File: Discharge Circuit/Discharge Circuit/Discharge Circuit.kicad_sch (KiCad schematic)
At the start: 6 parts, among them J1 MPT-02-01-XX-X-RA-SD, J2 IPBT-102-H1-T-S-RA-K, J3 PET-02-01-T-VT-LC, K2 FTR-E1AA012Y-GR

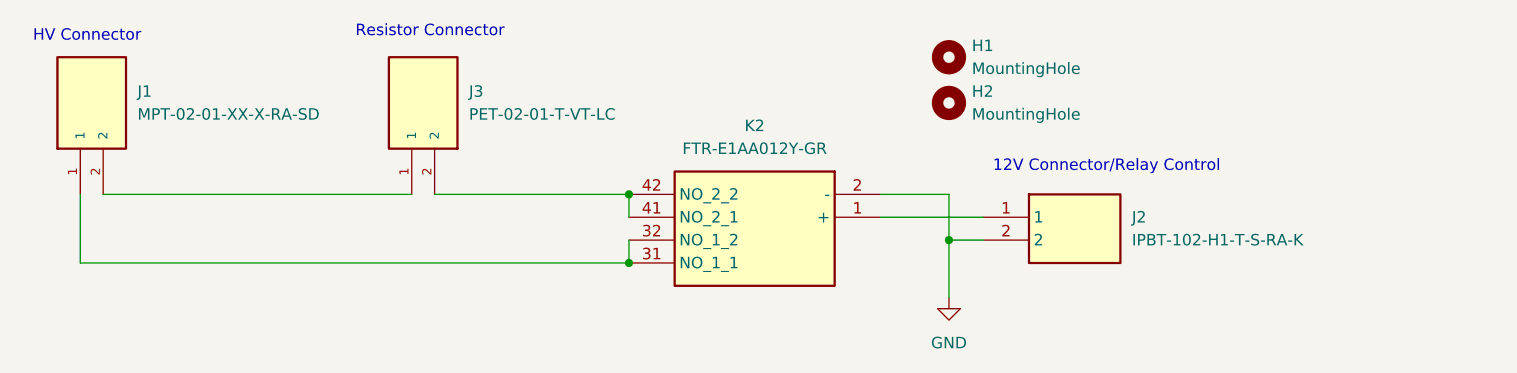
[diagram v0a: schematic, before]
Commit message: Added flyback diode
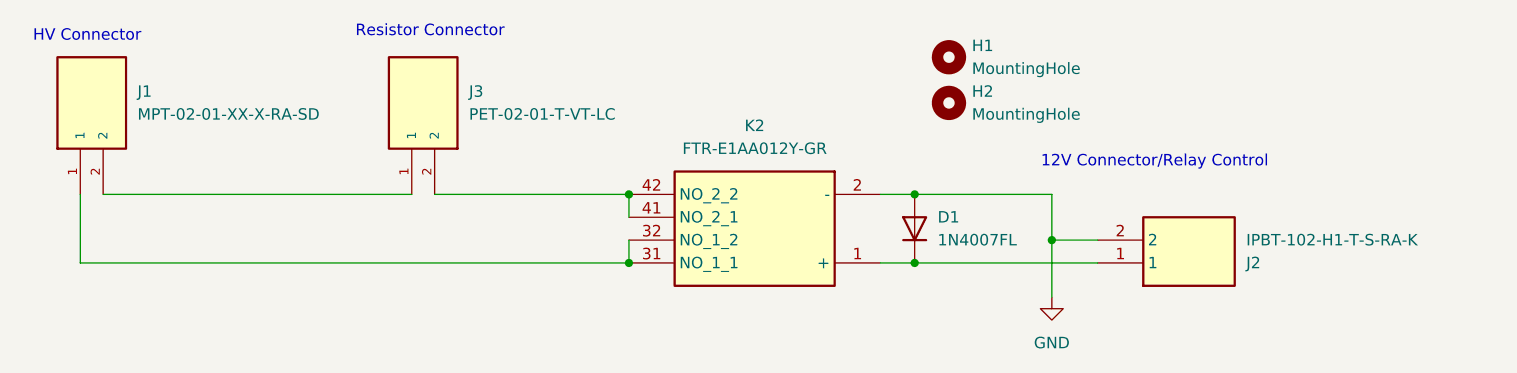
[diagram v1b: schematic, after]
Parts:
- added D1: 1N4007FL, Diode_SMD:D_SOD-123F, symbol Device:D
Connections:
- net GND: now also D1.2 (A)
- net at J2.1, K2.1 (+): now also D1.1 (K)
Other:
- moved on the sheet: J2
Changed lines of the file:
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@@
 	(text "12V Connector/Relay Control\n\n"
 		(exclude_from_sim no)
-		(at 183.896 108.458 0)
+		(at 189.23 107.95 0)
 		(effects
 			(font
@@
 	)
 	(junction
-		(at 166.37 115.57)
+		(at 130.81 118.11)
 		(diameter 0)
 		(color 0 0 0 0)
 	)
 	(junction
-		(at 130.81 118.11)
+		(at 177.8 115.57)
+		(diameter 0)
+		(color 0 0 0 0)
+	)
+	(junction
+		(at 162.56 118.11)
 		(diameter 0)
 		(color 0 0 0 0)
@@
 		(color 0 0 0 0)
 	)
+	(junction
+		(at 162.56 110.49)
+		(diameter 0)
+		(color 0 0 0 0)
+	)
+	(wire
+		(pts
+			(xy 162.56 118.11) (xy 182.88 118.11)
+		)
+		(stroke
+			(width 0)
+			(type default)
+		)
+	)
 	(wire
 		(pts
@@
 	(wire
 		(pts
-			(xy 170.18 115.57) (xy 166.37 115.57)
+			(xy 158.75 118.11) (xy 162.56 118.11)
 		)
 		(stroke
@@
 	(wire
 		(pts
-			(xy 158.75 110.49) (xy 166.37 110.49)
-		)
-		(stroke
-			(width 0)
-			(type default)
-		)
-	)
-	(wire
-		(pts
-			(xy 166.37 115.57) (xy 166.37 121.92)
-		)
-		(stroke
-			(width 0)
-			(type default)
-		)
-	)
-	(wire
-		(pts
-			(xy 158.75 113.03) (xy 170.18 113.03)
+			(xy 177.8 115.57) (xy 177.8 121.92)
+		)
+		(stroke
+			(width 0)
+			(type default)
+		)
+	)
+	(wire
+		(pts
+			(xy 158.75 110.49) (xy 162.56 110.49)
 		)
 		(stroke
@@
 	(wire
 		(pts
-			(xy 166.37 110.49) (xy 166.37 115.57)
+			(xy 162.56 110.49) (xy 177.8 110.49)
+		)
+		(stroke
+			(width 0)
+			(type default)
+		)
+	)
+	(wire
+		(pts
+			(xy 177.8 110.49) (xy 177.8 115.57)
+		)
+		(stroke
+			(width 0)
+			(type default)
+		)
+	)
+	(wire
+		(pts
+			(xy 182.88 115.57) (xy 177.8 115.57)
 		)
 		(stroke
@@
 	(symbol
 		(lib_id "power:GND")
-		(at 166.37 121.92 0)
+		(at 177.8 121.92 0)
 		(unit 1)
 		(exclude_from_sim no)
@@
 		(fields_autoplaced yes)
 		(property "Reference" "#PWR01"
-			(at 166.37 128.27 0)
+			(at 177.8 128.27 0)
 			(effects
 				(font
@@
 		)
 		(property "Value" "GND"
-			(at 166.37 127 0)
+			(at 177.8 127 0)
 			(effects
 				(font
@@
 		)
 		(property "Footprint" ""
-			(at 166.37 121.92 0)
+			(at 177.8 121.92 0)
 			(effects
 				(font
@@
 		)
 		(property "Datasheet" ""
-			(at 166.37 121.92 0)
+			(at 177.8 121.92 0)
 			(effects
 				(font
@@
 		)
 		(property "Description" "Power symbol creates a global label with name \"GND\" , ground"
-			(at 166.37 121.92 0)
+			(at 177.8 121.92 0)
 			(effects
 				(font
@@
 	(symbol
 		(lib_id "IPBT-102-H1-T-S-RA-K:IPBT-102-H1-T-S-RA-K")
-		(at 170.18 113.03 0)
+		(at 182.88 118.11 0)
+		(mirror x)
+		(unit 1)
+		(exclude_from_sim no)
+		(in_bom yes)
+		(on_board yes)
+		(dnp no)
+		(property "Reference" "J2"
+			(at 199.39 118.1101 0)
+			(effects
+				(font
+					(size 1.27 1.27)
+				)
+				(justify left)
+			)
+		)
+		(property "Value" "IPBT-102-H1-T-S-RA-K"
+			(at 199.39 115.5701 0)
+			(effects
+				(font
+					(size 1.27 1.27)
+				)
+				(justify left)
+			)
+		)
+		(property "Footprint" "IPBT:IPBT102H1TSRAK"
+			(at 199.39 23.19 0)
+			(effects
+				(font
+					(size 1.27 1.27)
+				)
+				(justify left top)
+				(hide yes)
+			)
+		)
+		(property "Datasheet" "https://suddendocs.samtec.com/prints/ipbt-1xx-xx-xx-s-xx-mkt.pdf?_gl=1*1nu67sl*_gcl_aw*R0NMLjE3MzY1MTU3OTIuQ2p3S0NBaUFwNE84QmhBa0Vpd0FxdjJVcUhrQ1hwTkVVY2dYbERaeHlmb2JUdHluT3BxNDdWZVFxUVNRZUFOZy1nZnhrUVhoSXppT0lob0NpMXdRQXZEX0J3RQ..*_gcl_au*NTMyOTAxMTM3LjE"
+			(at 199.39 -76.81 0)
+			(effects
+				(font
+					(size 1.27 1.27)
+				)
+				(justify left top)
+				(hide yes)
+			)
+		)
+		(property "Description" "Conn Power Mate Terminal Strip HDR 2 POS 4.19mm Solder RA Thru-Hole 2 Terminal 1 Port Automotive Tube"
+			(at 182.88 118.11 0)
+			(effects
+				(font
+					(size 1.27 1.27)
+				)
+				(hide yes)
+			)
+		)
+		(property "Height" "6.88"
+			(at 199.39 -276.81 0)
+			(effects
+				(font
+					(size 1.27 1.27)
+				)
+				(justify left top)
+				(hide yes)
+			)
+		)
+		(property "Mouser Part Number" "200-IPBT102H1TSRAK"
+			(at 199.39 -376.81 0)
+			(effects
+				(font
+					(size 1.27 1.27)
+				)
+				(justify left top)
+				(hide yes)
+			)
+		)
+		(property "Mouser Price/Stock" "https://www.mouser.co.uk/ProductDetail/Samtec/IPBT-102-H1-T-S-RA-K?qs=PB6%2FjmICvI2Ofyjz6y5btA%3D%3D"
+			(at 199.39 -476.81 0)
+			(effects
+				(font
+					(size 1.27 1.27)
+				)
+				(justify left top)
+				(hide yes)
+			)
+		)
+		(property "Manufacturer_Name" "SAMTEC"
+			(at 199.39 -576.81 0)
+			(effects
+				(font
+					(size 1.27 1.27)
+				)
+				(justify left top)
+				(hide yes)
+			)
+		)
+		(property "Manufacturer_Part_Number" "IPBT-102-H1-T-S-RA-K"
+			(at 199.39 -676.81 0)
+			(effects
+				(font
+					(size 1.27 1.27)
+				)
+				(justify left top)
+				(hide yes)
+			)
+		)
+		(pin "1"
+		)
+		(pin "2"
+		)
+		(instances
+			(project ""
+				(path "/faa29c35-f02e-4949-b6d7-f81fa5cf50a8"
+					(reference "J2")
+					(unit 1)
+				)
+			)
+		)
+	)
+	(symbol
+		(lib_id "Device:D")
+		(at 162.56 114.3 90)
 		(unit 1)
 		(exclude_from_sim no)
@@
 		(dnp no)
 		(fields_autoplaced yes)
-		(property "Reference" "J2"
-			(at 186.69 113.0299 0)
-			(effects
-				(font
-					(size 1.27 1.27)
-				)
-				(justify left)
-			)
-		)
-		(property "Value" "IPBT-102-H1-T-S-RA-K"
-			(at 186.69 115.5699 0)
-			(effects
-				(font
-					(size 1.27 1.27)
-				)
-				(justify left)
-			)
-		)
-		(property "Footprint" "IPBT:IPBT102H1TSRAK"
-			(at 186.69 207.95 0)
-			(effects
-				(font
-					(size 1.27 1.27)
-				)
-				(justify left top)
-				(hide yes)
-			)
-		)
-		(property "Datasheet" "https://suddendocs.samtec.com/prints/ipbt-1xx-xx-xx-s-xx-mkt.pdf?_gl=1*1nu67sl*_gcl_aw*R0NMLjE3MzY1MTU3OTIuQ2p3S0NBaUFwNE84QmhBa0Vpd0FxdjJVcUhrQ1hwTkVVY2dYbERaeHlmb2JUdHluT3BxNDdWZVFxUVNRZUFOZy1nZnhrUVhoSXppT0lob0NpMXdRQXZEX0J3RQ..*_gcl_au*NTMyOTAxMTM3LjE"
-			(at 186.69 307.95 0)
-			(effects
-				(font
-					(size 1.27 1.27)
-				)
-				(justify left top)
-				(hide yes)
-			)
-		)
-		(property "Description" "Conn Power Mate Terminal Strip HDR 2 POS 4.19mm Solder RA Thru-Hole 2 Terminal 1 Port Automotive Tube"
-			(at 170.18 113.03 0)
-			(effects
-				(font
-					(size 1.27 1.27)
-				)
-				(hide yes)
-			)
-		)
-		(property "Height" "6.88"
-			(at 186.69 507.95 0)
-			(effects
-				(font
-					(size 1.27 1.27)
-				)
-				(justify left top)
-				(hide yes)
-			)
-		)
-		(property "Mouser Part Number" "200-IPBT102H1TSRAK"
-			(at 186.69 607.95 0)
-			(effects
-				(font
-					(size 1.27 1.27)
-				)
-				(justify left top)
-				(hide yes)
-			)
-		)
-		(property "Mouser Price/Stock" "https://www.mouser.co.uk/ProductDetail/Samtec/IPBT-102-H1-T-S-RA-K?qs=PB6%2FjmICvI2Ofyjz6y5btA%3D%3D"
-			(at 186.69 707.95 0)
-			(effects
-				(font
-					(size 1.27 1.27)
-				)
-				(justify left top)
-				(hide yes)
-			)
-		)
-		(property "Manufacturer_Name" "SAMTEC"
-			(at 186.69 807.95 0)
-			(effects
-				(font
-					(size 1.27 1.27)
-				)
-				(justify left top)
-				(hide yes)
-			)
-		)
-		(property "Manufacturer_Part_Number" "IPBT-102-H1-T-S-RA-K"
-			(at 186.69 907.95 0)
-			(effects
-				(font
-					(size 1.27 1.27)
-				)
-				(justify left top)
+		(property "Reference" "D1"
+			(at 165.1 113.0299 90)
+			(effects
+				(font
+					(size 1.27 1.27)
+				)
+				(justify right)
+			)
+		)
+		(property "Value" "1N4007FL"
+			(at 165.1 115.5699 90)
+			(effects
+				(font
+					(size 1.27 1.27)
+				)
+				(justify right)
+			)
+		)
+		(property "Footprint" "Diode_SMD:D_SOD-123F"
+			(at 162.56 114.3 0)
+			(effects
+				(font
+					(size 1.27 1.27)
+				)
+				(hide yes)
+			)
+		)
+		(property "Datasheet" "~"
+			(at 162.56 114.3 0)
+			(effects
+				(font
+					(size 1.27 1.27)
+				)
+				(hide yes)
+			)
+		)
+		(property "Description" "Diode"
+			(at 162.56 114.3 0)
+			(effects
+				(font
+					(size 1.27 1.27)
+				)
+				(hide yes)
+			)
+		)
+		(property "Sim.Device" "D"
+			(at 162.56 114.3 0)
+			(effects
+				(font
+					(size 1.27 1.27)
+				)
+				(hide yes)
+			)
+		)
+		(property "Sim.Pins" "1=K 2=A"
+			(at 162.56 114.3 0)
+			(effects
+				(font
+					(size 1.27 1.27)
+				)
 				(hide yes)
 			)
@@
 			(project ""
 				(path "/faa29c35-f02e-4949-b6d7-f81fa5cf50a8"
-					(reference "J2")
+					(reference "D1")
 					(unit 1)
 				)
